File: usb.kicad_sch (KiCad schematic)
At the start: 104 parts, among them J901 USB-C_GCT_USB4105-GF-A, J902 USB-C_GCT_USB4105-GF-A, Q901 PJE138K, Q902 SQS401EN-T1_BE3, Q903 SSM3J332R, Q904 PJE138K, T901 Choke_DLW21SN900SQ2L, T902 Choke_DLW21SN900SQ2L, U901 AP22615A_TSOT26, U902 93AA66C_SOIC, U903 AP62301_TSOT, U905 FT4233HPQ, U906 TUSB321RWBR, Y901 Resonator_12MHz_ABM8G

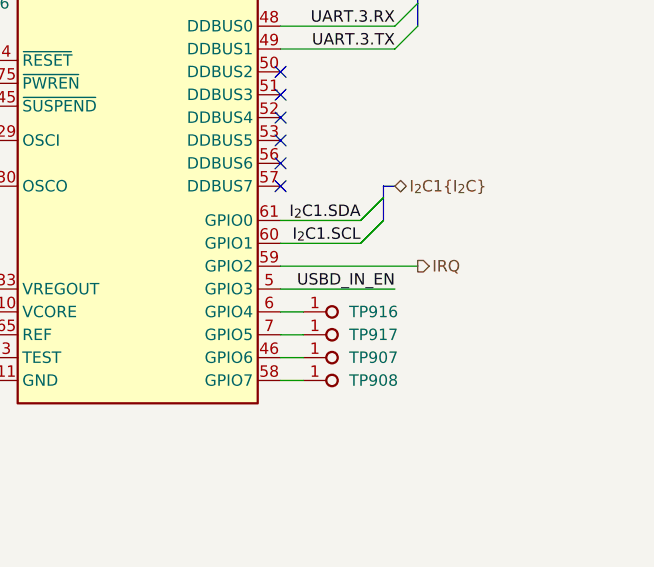
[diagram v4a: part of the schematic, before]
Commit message: [#58134] Remove I2C connection to FT4233
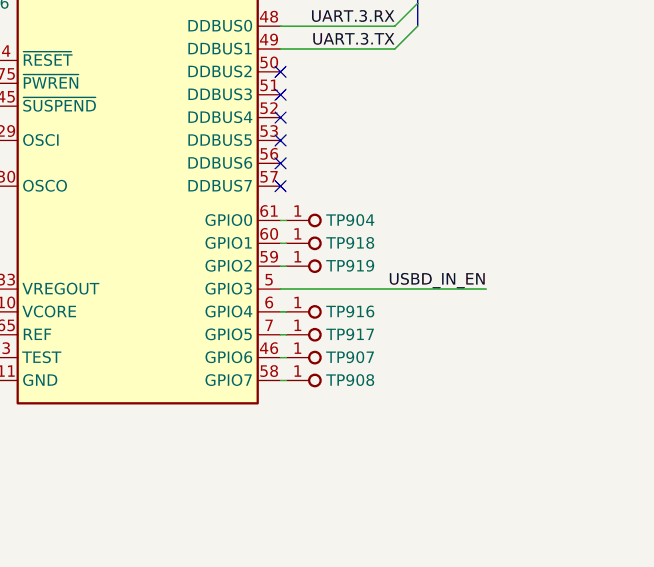
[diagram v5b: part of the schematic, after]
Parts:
- added TP904, TP918, TP919: TP_0.75mm_SMD, antmicro-footprints:TP_SMD_0.75mm, symbol antmicroTestPoints:TP_0.75mm_SMD
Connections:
- net IRQ: no longer names the net of U905.59 (GPIO2)
- net IRQ: now also TP919.1
- net I_{2}C1.SCL: no longer names the net of U905.60 (GPIO1)
- net I_{2}C1.SCL: now also TP918.1
- net I_{2}C1.SDA: no longer names the net of U905.61 (GPIO0)
- net I_{2}C1.SDA: now also TP904.1
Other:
- moved on the sheet: TP907, TP908, TP916, TP917

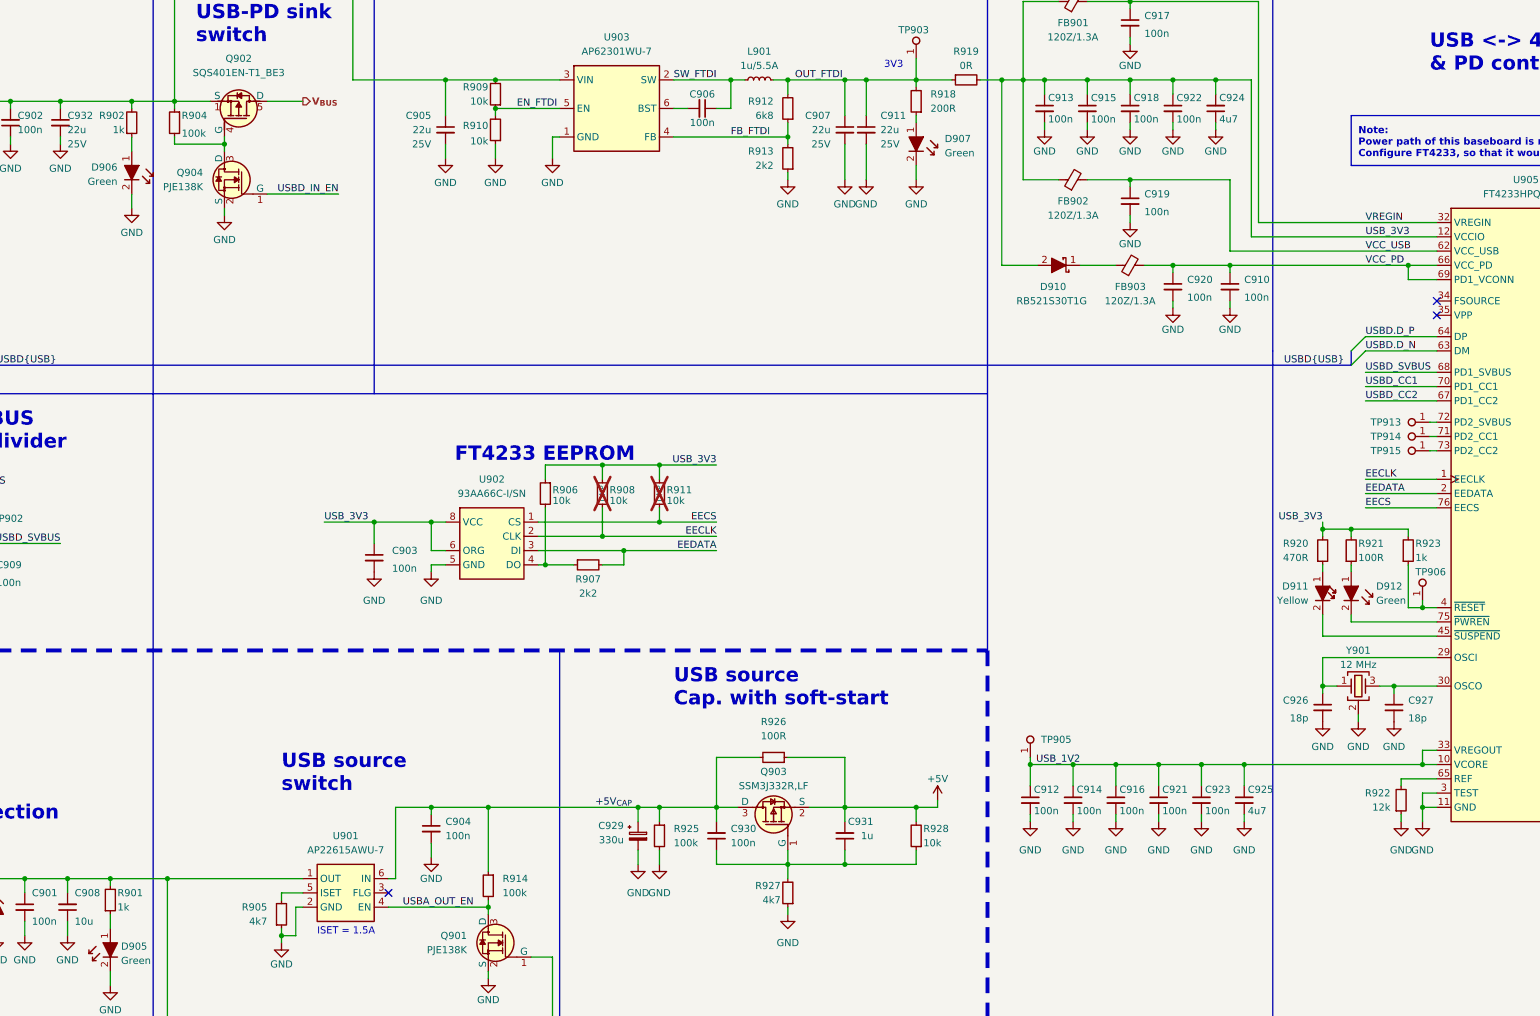
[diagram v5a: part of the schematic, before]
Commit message: [#58122] LED related fixes & improvements
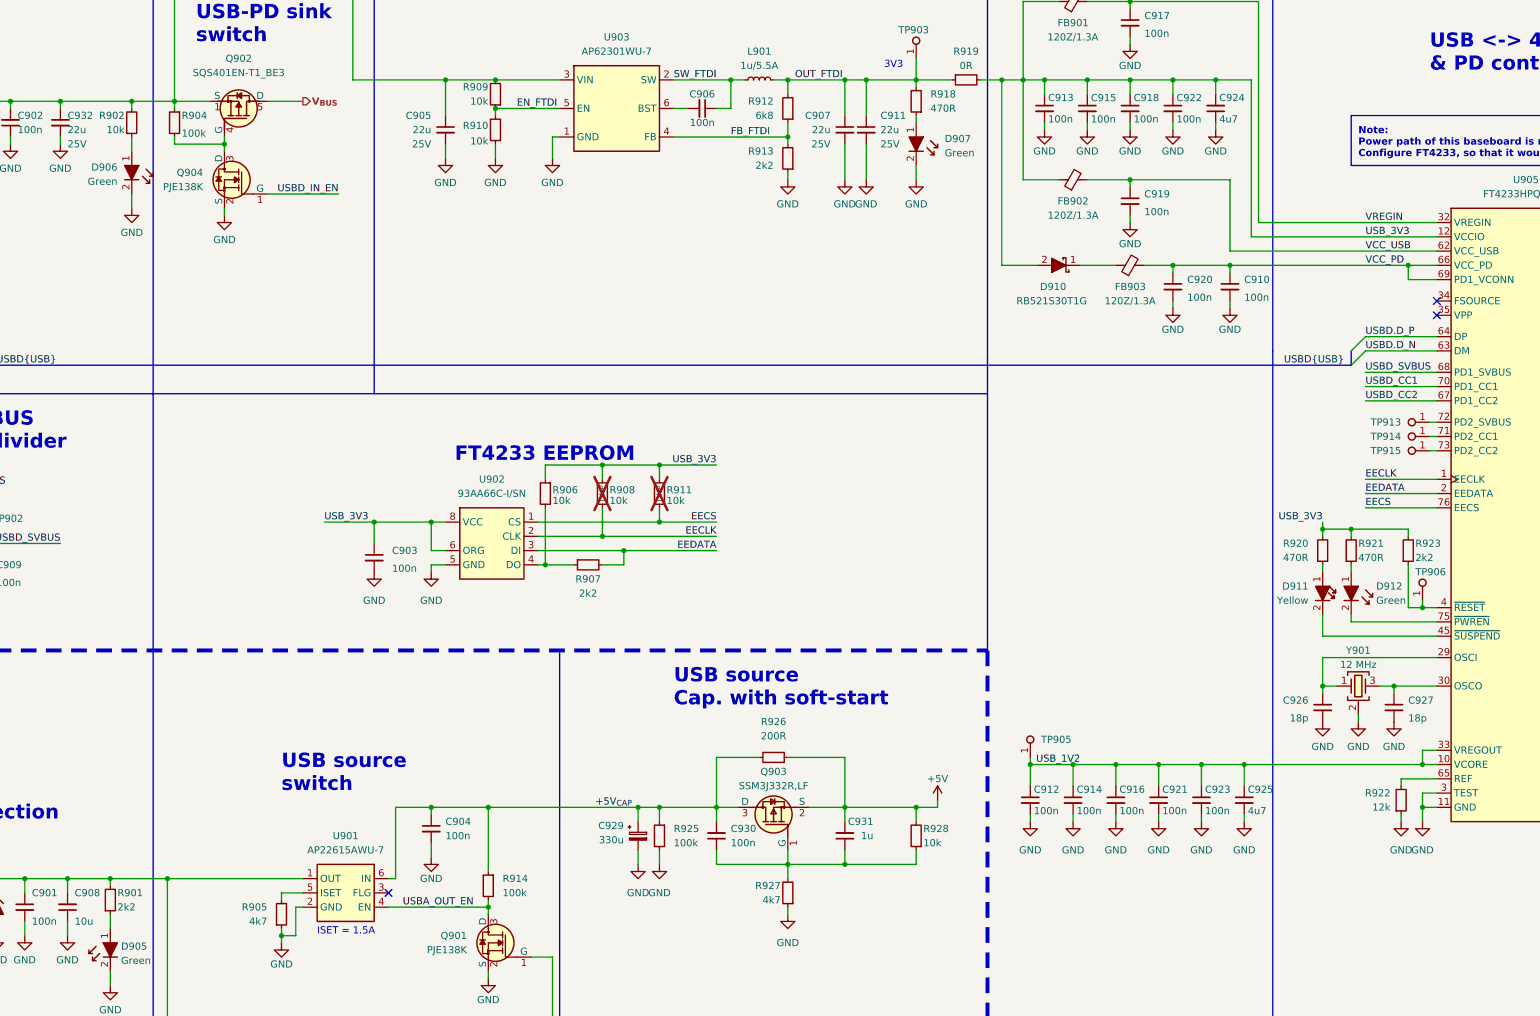
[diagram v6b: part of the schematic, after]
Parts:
- R901, R923: value R_1k_0402 -> R_2k2_0402; symbol antmicroResistors0402:R_1k_0402 -> antmicroResistors0402:R_2k2_0402; MPN CR0402-FX-1001GLF -> CR0402-FX-2201GLF; Val 1k -> 2k2
- R902: value R_1k_0402 -> R_10k_0402; symbol antmicroResistors0402:R_1k_0402 -> antmicroResistors0402:R_10k_0402; MPN CR0402-FX-1001GLF -> CR0402-FX-1002GLF; Val 1k -> 10k
- R918: value R_200R_0402 -> R_470R_0402; symbol antmicroResistors0402:R_200R_0402 -> antmicroResistors0402:R_470R_0402; MPN CR0402-FX-2000GLF -> CR0402-FX-4700GLF; Val 200R -> 470R
- R921: value R_100R_0402 -> R_470R_0402; symbol antmicroResistors0402:R_100R_0402 -> antmicroResistors0402:R_470R_0402; MPN CR0402-FX-1000GLF -> CR0402-FX-4700GLF; Val 100R -> 470R
- R926: value R_100R_0402 -> R_200R_0402; symbol antmicroResistors0402:R_100R_0402 -> antmicroResistors0402:R_200R_0402; MPN CR0402-FX-1000GLF -> CR0402-FX-2000GLF; Val 100R -> 200R
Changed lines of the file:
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@@
     )
   )
-  (symbol (lib_id "antmicroResistors0402:R_100R_0402") (at 220.98 175.26 180) (unit 1)
+  (symbol (lib_id "antmicroResistors0402:R_200R_0402") (at 220.98 175.26 180) (unit 1)
     (in_bom yes) (on_board yes) (dnp no) (fields_autoplaced)
     (property "Reference" "R926" (at 218.44 168.91 0)
       (effects (font (size 1.27 1.27) (thickness 0.15)))
     )
-    (property "Value" "R_100R_0402" (at 200.66 162.56 0)
+    (property "Value" "R_200R_0402" (at 200.66 162.56 0)
       (effects (font (size 1.27 1.27) (thickness 0.15)) (justify left bottom) hide)
     )
@@
       (effects (font (size 1.27 1.27) (thickness 0.15)) (justify left bottom) hide)
     )
-    (property "MPN" "CR0402-FX-1000GLF" (at 200.66 154.94 0)
+    (property "MPN" "CR0402-FX-2000GLF" (at 200.66 154.94 0)
       (effects (font (size 1.27 1.27) (thickness 0.15)) (justify left bottom) hide)
     )
@@
       (effects (font (size 1.27 1.27) (thickness 0.15)) (justify left bottom) hide)
     )
-    (property "Val" "100R" (at 218.44 171.45 0)
+    (property "Val" "200R" (at 218.44 171.45 0)
       (effects (font (size 1.27 1.27) (thickness 0.15)))
     )
@@
     )
   )
-  (symbol (lib_id "antmicroResistors0402:R_1k_0402") (at 104.14 64.77 90) (unit 1)
+  (symbol (lib_id "antmicroResistors0402:R_10k_0402") (at 104.14 64.77 90) (unit 1)
     (in_bom yes) (on_board yes) (dnp no)
     (property "Reference" "R902" (at 102.87 60.96 90)
       (effects (font (size 1.27 1.27) (thickness 0.15)) (justify left))
     )
-    (property "Value" "R_1k_0402" (at 116.84 44.45 0)
+    (property "Value" "R_10k_0402" (at 116.84 44.45 0)
       (effects (font (size 1.27 1.27) (thickness 0.15)) (justify left bottom) hide)
     )
@@
       (effects (font (size 1.27 1.27) (thickness 0.15)) (justify left bottom) hide)
     )
-    (property "MPN" "CR0402-FX-1001GLF" (at 124.46 44.45 0)
+    (property "MPN" "CR0402-FX-1002GLF" (at 124.46 44.45 0)
       (effects (font (size 1.27 1.27) (thickness 0.15)) (justify left bottom) hide)
     )
@@
       (effects (font (size 1.27 1.27) (thickness 0.15)) (justify left bottom) hide)
     )
-    (property "Val" "1k" (at 102.87 63.5 90)
+    (property "Val" "10k" (at 102.87 63.5 90)
       (effects (font (size 1.27 1.27) (thickness 0.15)) (justify left))
     )
@@
     )
   )
-  (symbol (lib_id "antmicroResistors0402:R_100R_0402") (at 321.31 140.97 90) (unit 1)
+  (symbol (lib_id "antmicroResistors0402:R_470R_0402") (at 321.31 140.97 90) (unit 1)
     (in_bom yes) (on_board yes) (dnp no)
     (property "Reference" "R921" (at 322.58 137.16 90)
       (effects (font (size 1.27 1.27) (thickness 0.15)) (justify right))
     )
-    (property "Value" "R_100R_0402" (at 334.01 120.65 0)
+    (property "Value" "R_470R_0402" (at 334.01 120.65 0)
       (effects (font (size 1.27 1.27) (thickness 0.15)) (justify left bottom) hide)
     )
@@
       (effects (font (size 1.27 1.27) (thickness 0.15)) (justify left bottom) hide)
     )
-    (property "MPN" "CR0402-FX-1000GLF" (at 341.63 120.65 0)
+    (property "MPN" "CR0402-FX-4700GLF" (at 341.63 120.65 0)
       (effects (font (size 1.27 1.27) (thickness 0.15)) (justify left bottom) hide)
     )
@@
       (effects (font (size 1.27 1.27) (thickness 0.15)) (justify left bottom) hide)
     )
-    (property "Val" "100R" (at 322.58 139.7 90)
+    (property "Val" "470R" (at 322.58 139.7 90)
       (effects (font (size 1.27 1.27) (thickness 0.15)) (justify right))
     )
@@
     )
   )
-  (symbol (lib_id "antmicroResistors0402:R_1k_0402") (at 100.33 203.2 90) (unit 1)
+  (symbol (lib_id "antmicroResistors0402:R_2k2_0402") (at 100.33 203.2 90) (unit 1)
     (in_bom yes) (on_board yes) (dnp no)
     (property "Reference" "R901" (at 101.6 199.39 90)
       (effects (font (size 1.27 1.27) (thickness 0.15)) (justify right))
     )
-    (property "Value" "R_1k_0402" (at 113.03 182.88 0)
+    (property "Value" "R_2k2_0402" (at 113.03 182.88 0)
       (effects (font (size 1.27 1.27) (thickness 0.15)) (justify left bottom) hide)
     )
@@
       (effects (font (size 1.27 1.27) (thickness 0.15)) (justify left bottom) hide)
     )
-    (property "MPN" "CR0402-FX-1001GLF" (at 120.65 182.88 0)
+    (property "MPN" "CR0402-FX-2201GLF" (at 120.65 182.88 0)
       (effects (font (size 1.27 1.27) (thickness 0.15)) (justify left bottom) hide)
     )
@@
       (effects (font (size 1.27 1.27) (thickness 0.15)) (justify left bottom) hide)
     )
-    (property "Val" "1k" (at 101.6 201.93 90)
+    (property "Val" "2k2" (at 101.6 201.93 90)
       (effects (font (size 1.27 1.27) (thickness 0.15)) (justify right))
     )
@@
     )
   )
-  (symbol (lib_id "antmicroResistors0402:R_200R_0402") (at 243.84 60.96 270) (mirror x) (unit 1)
+  (symbol (lib_id "antmicroResistors0402:R_470R_0402") (at 243.84 60.96 270) (mirror x) (unit 1)
     (in_bom yes) (on_board yes) (dnp no) (fields_autoplaced)
     (property "Reference" "R918" (at 246.38 57.1499 90)
       (effects (font (size 1.27 1.27)) (justify left))
     )
-    (property "Value" "R_200R_0402" (at 231.14 40.64 0)
+    (property "Value" "R_470R_0402" (at 231.14 40.64 0)
       (effects (font (size 1.27 1.27) (thickness 0.15)) (justify left bottom) hide)
     )
@@
       (effects (font (size 1.27 1.27) (thickness 0.15)) (justify left bottom) hide)
     )
-    (property "MPN" "CR0402-FX-2000GLF" (at 223.52 40.64 0)
+    (property "MPN" "CR0402-FX-4700GLF" (at 223.52 40.64 0)
       (effects (font (size 1.27 1.27) (thickness 0.15)) (justify left bottom) hide)
     )
-    (property "Val" "200R" (at 246.38 59.6899 90)
+    (property "Val" "470R" (at 246.38 59.6899 90)
       (effects (font (size 1.27 1.27) (thickness 0.15)) (justify left))
     )
@@
     )
   )
-  (symbol (lib_id "antmicroResistors0402:R_1k_0402") (at 331.47 140.97 90) (unit 1)
+  (symbol (lib_id "antmicroResistors0402:R_2k2_0402") (at 331.47 140.97 90) (unit 1)
     (in_bom yes) (on_board yes) (dnp no)
     (property "Reference" "R923" (at 332.74 137.16 90)
       (effects (font (size 1.27 1.27) (thickness 0.15)) (justify right))
     )
-    (property "Value" "R_1k_0402" (at 344.17 120.65 0)
+    (property "Value" "R_2k2_0402" (at 344.17 120.65 0)
       (effects (font (size 1.27 1.27) (thickness 0.15)) (justify left bottom) hide)
     )
@@
       (effects (font (size 1.27 1.27) (thickness 0.15)) (justify left bottom) hide)
     )
-    (property "MPN" "CR0402-FX-1001GLF" (at 351.79 120.65 0)
+    (property "MPN" "CR0402-FX-2201GLF" (at 351.79 120.65 0)
       (effects (font (size 1.27 1.27) (thickness 0.15)) (justify left bottom) hide)
     )
@@
       (effects (font (size 1.27 1.27) (thickness 0.15)) (justify left bottom) hide)
     )
-    (property "Val" "1k" (at 332.74 139.7 90)
+    (property "Val" "2k2" (at 332.74 139.7 90)
       (effects (font (size 1.27 1.27) (thickness 0.15)) (justify right))
     )
